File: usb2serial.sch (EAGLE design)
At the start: 16 parts, among them IC1 FT232RL

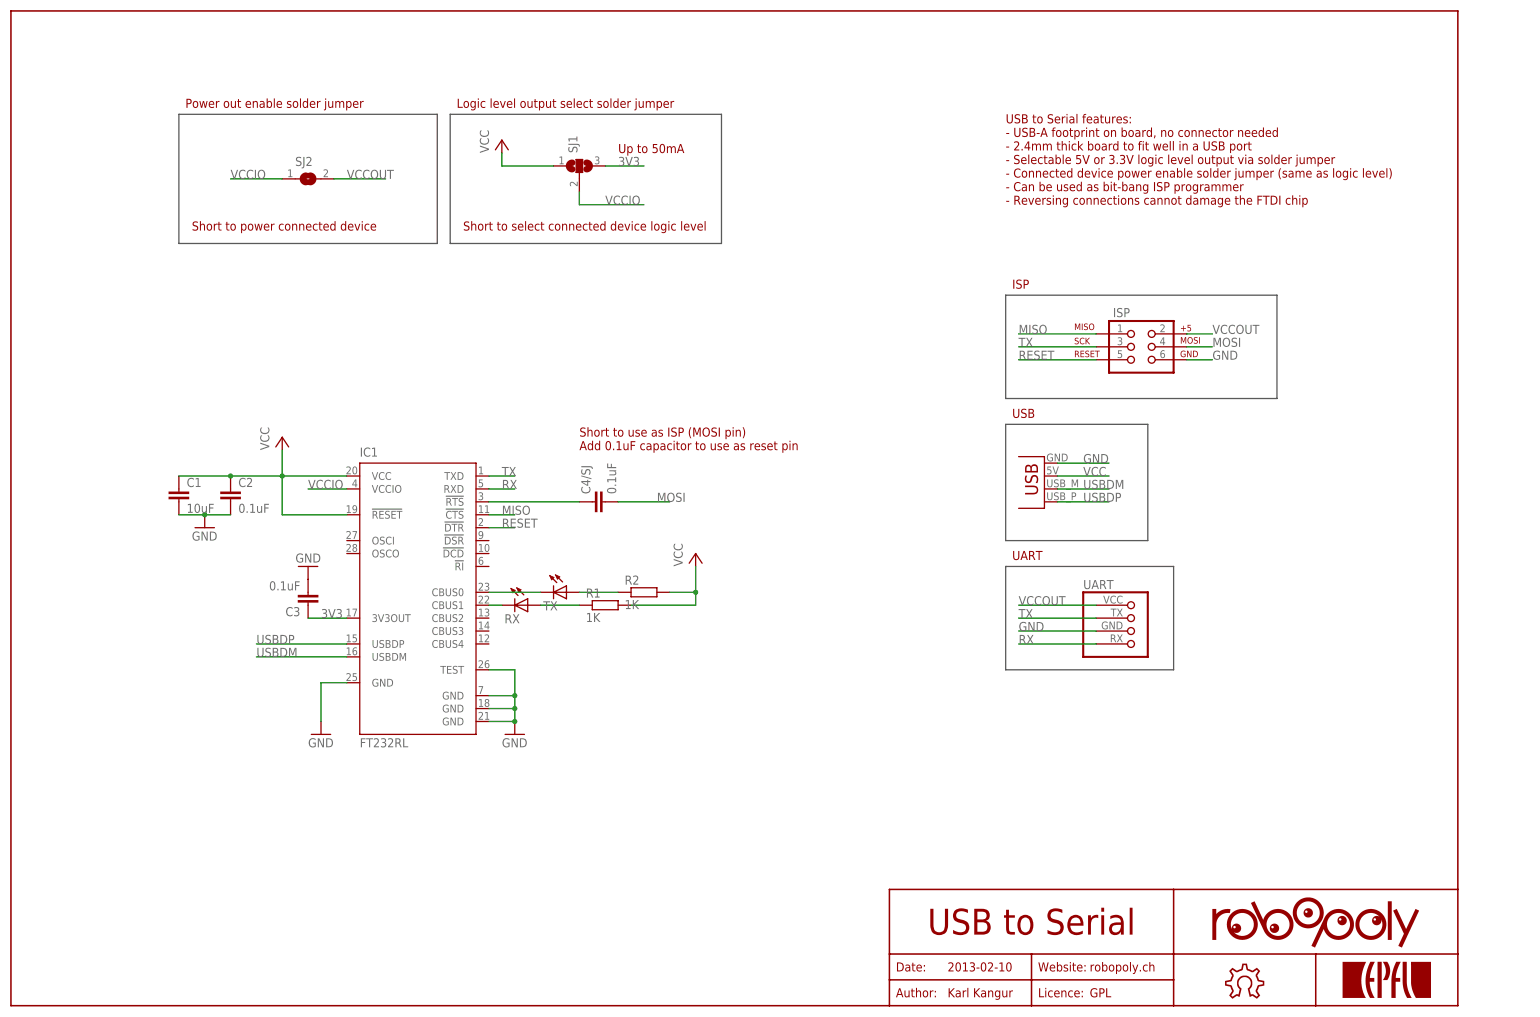
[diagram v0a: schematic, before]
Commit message: Replaced the FT232R with FT230X chip
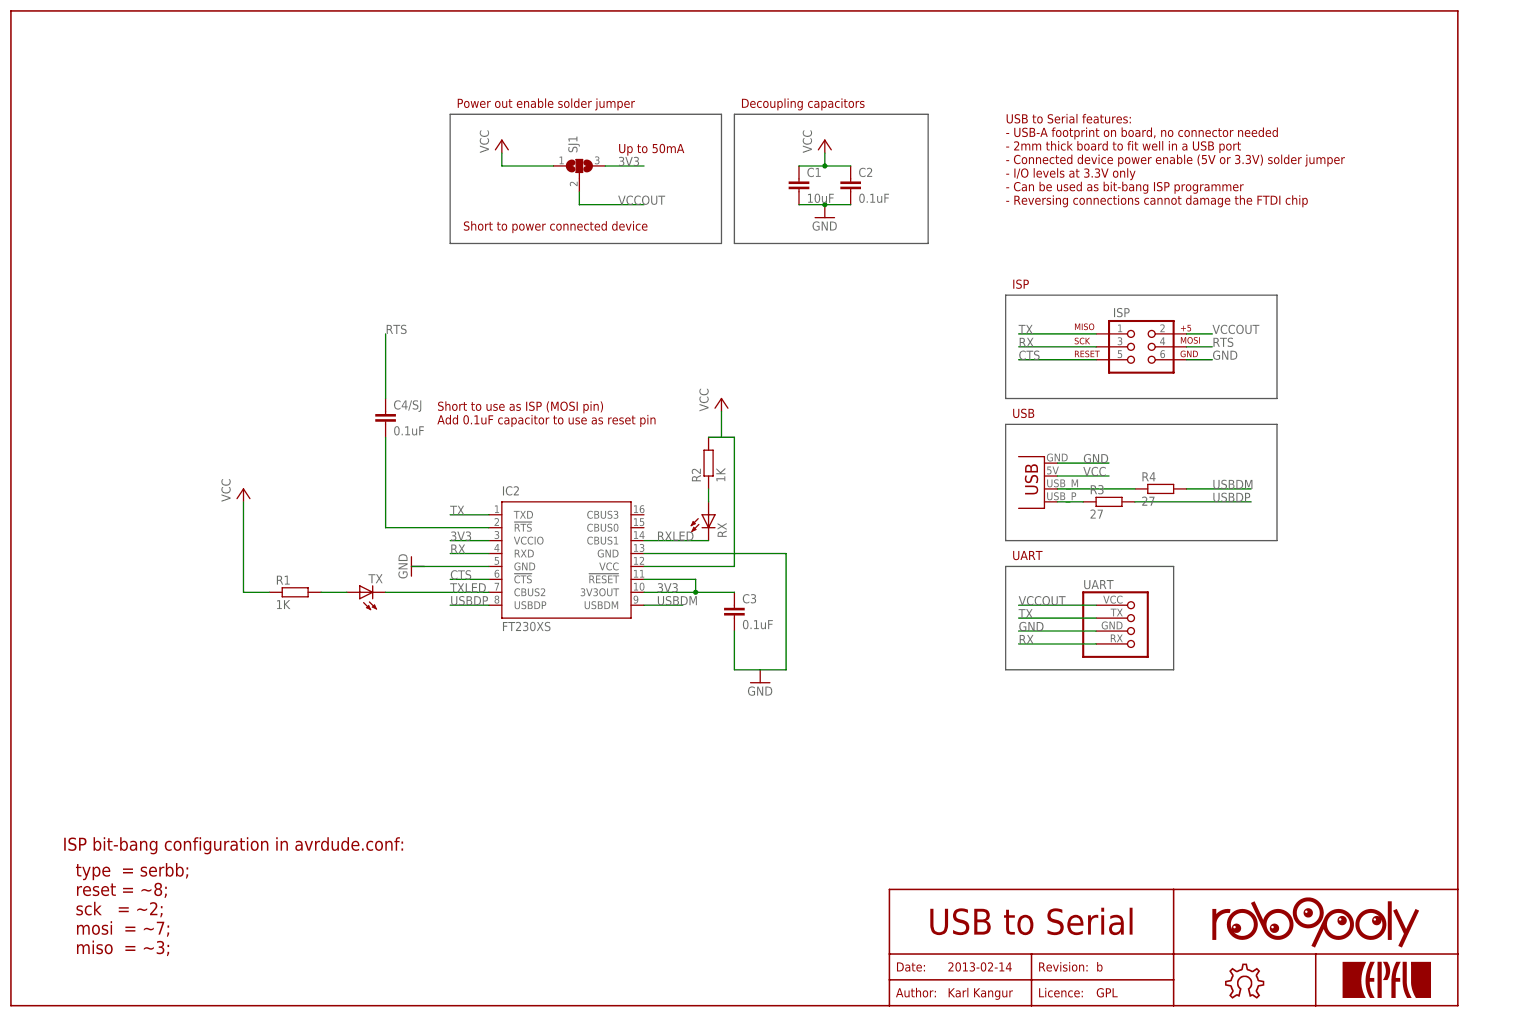
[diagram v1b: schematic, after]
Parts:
- removed IC1: FT232RL, ftdichip:FT232RL
- removed SJ2: (no value), jumper:SJ
- added IC2: FT230XS, ftdichip:FT230XS
- added R3, R4: 27, rcl:R-EU_R0805
- U$1: value UART-ROBOPOLY -> UART-ROBOPOLY90; device karl:UART-ROBOPOLY -> karl:UART-ROBOPOLY90
- U$3: value OPEN-HARDWARE-LOGOBOTTOM -> OPEN-HARDWARE-LOGOBOTTOM-SMALL; device karl:OPEN-HARDWARE-LOGOBOTTOM -> karl:OPEN-HARDWARE-LOGOBOTTOM-SMALL
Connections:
- removed net MISO: IC1.!CTS, ISP.1
- removed net MOSI: C4/SJ.2, ISP.4
- removed net N$5: IC1.CBUS1, RX.C
- removed net N$7: R1.1, RX.A
- removed net RESET: IC1.!DTR, ISP.5
- removed net VCCIO: IC1.VCCIO, SJ1.2, SJ2.1
- new net CTS: IC2.!CTS, ISP.5
- new net N$2: R1.2, TX.A
- new net N$3: C4/SJ.2, IC2.!RTS
- new net RTS: C4/SJ.1, ISP.4
- new net RXLED: IC2.CBUS1, RX.C
- new net TXLED: IC2.CBUS2, TX.C
- net 3V3: now also IC2.!RESET, IC2.3V3OUT, IC2.VCCIO; no longer IC1.3V3OUT
- net GND: now also IC2.GND, IC2.GND@1; no longer IC1.GND, IC1.GND@1, IC1.GND@2, IC1.GND@A, IC1.TEST
- net N$1: now also JP1.D-, R4.1; no longer C4/SJ.1, IC1.!RTS
- net N$4: now also RX.A; no longer TX.A
- net N$6: now also JP1.D+, R3.1; no longer IC1.CBUS0, TX.C
- net RX: now also IC2.RXD, ISP.3; no longer IC1.RXD
- net TX: now also IC2.TXD, ISP.1; no longer IC1.TXD, ISP.3
- net USBDM: now also IC2.USBDM, R4.2; no longer IC1.USBDM, JP1.D-
- net USBDP: now also IC2.USBDP, R3.2; no longer IC1.USBDP, JP1.D+
- net VCC: now also IC2.VCC, R1.1; no longer IC1.!RESET, IC1.VCC, R1.2
- net VCCOUT: now also SJ1.2; no longer SJ2.2
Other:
- note added: "2013-02-14"
- note added: "Decoupling capacitors"
- note added: "ISP bit-bang configuration in avrdude.conf:"
- note added: "Revision:"
- note added: "USB to Serial features: - USB-A footprint on board, no connector needed - 2mm thick board to fit well in a USB port - Connected device power enable (5V or 3.3V) solder jumper - I/O levels at 3.3V only - Can be used as bit-bang ISP programmer - Reversing connections cannot damage the FTDI chip"
- note added: "b"
- note added: "type = serbb; reset = ~8; sck = ~2; mosi = ~7; miso = ~3;"
- note removed: "2013-02-10"
- note removed: "Logic level output select solder jumper"
- note removed: "Short to select connected device logic level"
- note removed: "USB to Serial features: - USB-A footprint on board, no connector needed - 2.4mm thick board to fit well in a USB port - Selectable 5V or 3.3V logic level output via solder jumper - Connected device power enable solder jumper (same as logic level) - Can be used as bit-bang ISP programmer - Reversing connections cannot damage the FTDI chip"
- note removed: "Website:"
- note removed: "robopoly.ch"
- moved on the sheet: C1, C2, C3, C4/SJ, R1, R2, RX, TX
